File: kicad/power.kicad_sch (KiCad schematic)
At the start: 39 parts, among them Q201 AOD409, U201 TPS54331, U202 AMS1117-3.3

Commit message: Update to v1.1.0
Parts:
- C201: JLCPCB Part # (none) -> C109394
- C202, C203, C210, C211: JLCPCB Part # (none) -> C96446
- C204, C206: JLCPCB Part # (none) -> C57112
- C205: JLCPCB Part # (none) -> C1588
- C207: JLCPCB Part # (none) -> C1679
- C208: JLCPCB Part # (none) -> C107045
- C209, C212: JLCPCB Part # (none) -> C14663
- C213, C214: JLCPCB Part # (none) -> C8020
- D201: JLCPCB Part # (none) -> C110044
- D202: JLCPCB Part # (none) -> C8062
- D203: JLCPCB Part # (none) -> C8678
- D204: JLCPCB Part # (none) -> C142303
- F202: JLCPCB Part # (none) -> C883107
- F501: JLCPCB Part # (none) -> C883133
- L201: JLCPCB Part # (none) -> C68434
- L202: JLCPCB Part # (none) -> C1015
- Q201: JLCPCB Part # (none) -> C36220
- R201, R202, R204, R205, R207: JLCPCB Part # (none) -> C25804
- R203: JLCPCB Part # (none) -> C25803
- R206: JLCPCB Part # (none) -> C23212
- R208: JLCPCB Part # (none) -> C22808
- R209: JLCPCB Part # (none) -> C4177
- R210: JLCPCB Part # (none) -> C23138
- U201: JLCPCB Part # (none) -> C9865
- U202: JLCPCB Part # (none) -> C6186
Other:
- company: BlueDot, Vincenzo Fortunato -> BlueDot Arcade, Vincenzo Fortunato
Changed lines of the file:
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@@
   (title_block
     (title "BD845-PWB SCH")
-    (date "2022-11-27")
-    (rev "1.0.0")
-    (company "BlueDot, Vincenzo Fortunato")
+    (date "2023-06-14")
+    (rev "1.1.0")
+    (company "BlueDot Arcade, Vincenzo Fortunato")
+    (comment 1 "bluedotarcade.com")
   )
   (junction (at 85.09 125.73) (diameter 0) (color 0 0 0 0)
@@
     )
     (property "Datasheet" "~" (at 85.09 121.92 0)
+      (effects (font (size 1.27 1.27)) hide)
+    )
+    (property "JLCPCB Part #" "C25804" (at 85.09 121.92 0)
       (effects (font (size 1.27 1.27)) hide)
     )
@@
     (property "Datasheet" "https://datasheet.lcsc.com/lcsc/1811091710_Alpha---Omega-Semicon-AOD409_C36220.pdf" (at 53.34 55.88 0)
       (effects (font (size 1.27 1.27)) (justify left) hide)
+    )
+    (property "JLCPCB Part #" "C36220" (at 53.34 55.88 0)
+      (effects (font (size 1.27 1.27)) hide)
     )
     (pin "1")
@@
       (effects (font (size 1.27 1.27)) hide)
     )
+    (property "JLCPCB Part #" "C110044" (at 38.1 59.69 0)
+      (effects (font (size 1.27 1.27)) hide)
+    )
     (pin "1")
     (pin "2")
@@
       (effects (font (size 1.27 1.27)))
     )
+    (property "JLCPCB Part #" "C25804" (at 179.07 115.57 0)
+      (effects (font (size 1.27 1.27)) hide)
+    )
     (pin "1")
     (pin "2")
@@
       (effects (font (size 1.27 1.27)) (justify left))
     )
+    (property "JLCPCB Part #" "C8020" (at 118.11 63.5 0)
+      (effects (font (size 1.27 1.27)) hide)
+    )
     (pin "1")
     (pin "2")
@@
       (effects (font (size 1.27 1.27)) hide)
     )
+    (property "JLCPCB Part #" "C96446" (at 189.23 107.95 0)
+      (effects (font (size 1.27 1.27)) hide)
+    )
     (pin "1")
     (pin "2")
@@
     )
     (property "Datasheet" "~" (at 54.61 114.3 0)
+      (effects (font (size 1.27 1.27)) hide)
+    )
+    (property "JLCPCB Part #" "C96446" (at 54.61 114.3 0)
       (effects (font (size 1.27 1.27)) hide)
     )
@@
       (effects (font (size 1.27 1.27)) hide)
     )
+    (property "JLCPCB Part #" "" (at 167.64 58.42 0)
+      (effects (font (size 1.27 1.27)) hide)
+    )
     (pin "1")
     (instances
@@
     )
     (property "Datasheet" "~" (at 166.37 107.95 90)
+      (effects (font (size 1.27 1.27)) hide)
+    )
+    (property "JLCPCB Part #" "C8678" (at 166.37 107.95 0)
       (effects (font (size 1.27 1.27)) hide)
     )
@@
       (effects (font (size 1.27 1.27)) hide)
     )
+    (property "JLCPCB Part #" "C1015" (at 113.03 58.42 0)
+      (effects (font (size 1.27 1.27)) hide)
+    )
     (pin "1")
     (pin "2")
@@
       (effects (font (size 1.27 1.27)) hide)
     )
+    (property "JLCPCB Part #" "C57112" (at 64.77 114.3 0)
+      (effects (font (size 1.27 1.27)) hide)
+    )
     (pin "1")
     (pin "2")
@@
       (effects (font (size 1.27 1.27)) (justify left))
     )
+    (property "JLCPCB Part #" "C23212" (at 115.57 128.27 0)
+      (effects (font (size 1.27 1.27)) hide)
+    )
     (pin "1")
     (pin "2")
@@
     )
     (property "Datasheet" "~" (at 44.45 114.3 0)
+      (effects (font (size 1.27 1.27)) hide)
+    )
+    (property "JLCPCB Part #" "C96446" (at 44.45 114.3 0)
       (effects (font (size 1.27 1.27)) hide)
     )
@@
       (effects (font (size 1.27 1.27)) hide)
     )
+    (property "JLCPCB Part #" "C6186" (at 134.62 58.42 0)
+      (effects (font (size 1.27 1.27)) hide)
+    )
     (pin "1")
     (pin "2")
@@
     )
     (property "Datasheet" "https://www.ti.com/lit/ds/symlink/tps54331.pdf" (at 154.94 127 0)
+      (effects (font (size 1.27 1.27)) hide)
+    )
+    (property "JLCPCB Part #" "C9865" (at 129.54 115.57 0)
       (effects (font (size 1.27 1.27)) hide)
     )
@@
       (effects (font (size 1.27 1.27)) hide)
     )
+    (property "JLCPCB Part #" "C107045" (at 115.57 135.89 0)
+      (effects (font (size 1.27 1.27)) hide)
+    )
     (pin "1")
     (pin "2")
@@
       (effects (font (size 1.27 1.27)) hide)
     )
+    (property "JLCPCB Part #" "C57112" (at 96.52 127 0)
+      (effects (font (size 1.27 1.27)) hide)
+    )
     (pin "1")
     (pin "2")
@@
     (property "Accuracy" "1%" (at 181.61 137.16 0)
       (effects (font (size 1.27 1.27)) (justify left))
+    )
+    (property "JLCPCB Part #" "C4177" (at 179.07 134.62 0)
+      (effects (font (size 1.27 1.27)) hide)
     )
     (pin "1")
@@
       (effects (font (size 1.27 1.27)) hide)
     )
+    (property "JLCPCB Part #" "C25804" (at 53.34 64.77 0)
+      (effects (font (size 1.27 1.27)) hide)
+    )
     (pin "1")
     (pin "2")
@@
     (property "ESR" "10Ω" (at 153.67 66.04 0)
       (effects (font (size 1.27 1.27)) (justify left))
+    )
+    (property "JLCPCB Part #" "C8020" (at 151.13 63.5 0)
+      (effects (font (size 1.27 1.27)) hide)
     )
     (pin "1")
@@
       (effects (font (size 1.27 1.27)) hide)
     )
+    (property "JLCPCB Part #" "C883107" (at 160.02 58.42 0)
+      (effects (font (size 1.27 1.27)) hide)
+    )
     (pin "1")
     (pin "2")
@@
       (effects (font (size 1.27 1.27)) hide)
     )
+    (property "JLCPCB Part #" "C8062" (at 60.96 57.15 0)
+      (effects (font (size 1.27 1.27)) hide)
+    )
     (pin "1")
     (pin "2")
@@
     (property "Accuracy" "1%" (at 182.88 128.27 0)
       (effects (font (size 1.27 1.27)))
+    )
+    (property "JLCPCB Part #" "C22808" (at 179.07 125.73 0)
+      (effects (font (size 1.27 1.27)) hide)
     )
     (pin "1")
@@
       (effects (font (size 1.27 1.27)) hide)
     )
+    (property "JLCPCB Part #" "C25803" (at 85.09 114.3 0)
+      (effects (font (size 1.27 1.27)) hide)
+    )
     (pin "1")
     (pin "2")
@@
       (effects (font (size 1.27 1.27)) hide)
     )
+    (property "JLCPCB Part #" "C23138" (at 204.47 69.85 0)
+      (effects (font (size 1.27 1.27)) hide)
+    )
     (pin "1")
     (pin "2")
@@
       (effects (font (size 1.27 1.27)))
     )
+    (property "JLCPCB Part #" "C68434" (at 172.72 102.87 0)
+      (effects (font (size 1.27 1.27)) hide)
+    )
     (pin "1")
     (pin "2")
@@
     )
     (property "Datasheet" "~" (at 107.95 63.5 0)
+      (effects (font (size 1.27 1.27)) hide)
+    )
+    (property "JLCPCB Part #" "C14663" (at 107.95 63.5 0)
       (effects (font (size 1.27 1.27)) hide)
     )
@@
       (effects (font (size 1.27 1.27)) hide)
     )
+    (property "JLCPCB Part #" "C142303" (at 204.47 49.53 0)
+      (effects (font (size 1.27 1.27)) hide)
+    )
     (pin "1")
     (pin "2")
@@
       (effects (font (size 1.27 1.27)) hide)
     )
+    (property "JLCPCB Part #" "C25804" (at 74.93 129.54 0)
+      (effects (font (size 1.27 1.27)) hide)
+    )
     (pin "1")
     (pin "2")
@@
     )
     (property "Datasheet" "~" (at 74.93 114.3 0)
+      (effects (font (size 1.27 1.27)) hide)
+    )
+    (property "JLCPCB Part #" "C1588" (at 74.93 114.3 0)
       (effects (font (size 1.27 1.27)) hide)
     )
@@
       (effects (font (size 1.27 1.27)) hide)
     )
+    (property "JLCPCB Part #" "C883133" (at 38.1 110.49 0)
+      (effects (font (size 1.27 1.27)) hide)
+    )
     (pin "1")
     (pin "2")
@@
       (effects (font (size 1.27 1.27)) hide)
     )
+    (property "JLCPCB Part #" "C96446" (at 199.39 107.95 0)
+      (effects (font (size 1.27 1.27)) hide)
+    )
     (pin "1")
     (pin "2")
@@
     (property "ESR" "1mΩ" (at 156.21 106.68 90)
       (effects (font (size 1.27 1.27)))
+    )
+    (property "JLCPCB Part #" "C14663" (at 156.21 110.49 0)
+      (effects (font (size 1.27 1.27)) hide)
     )
     (pin "1")
@@
       (effects (font (size 1.27 1.27)) hide)
     )
+    (property "JLCPCB Part #" "" (at 72.39 53.34 0)
+      (effects (font (size 1.27 1.27)) hide)
+    )
     (pin "1")
     (instances
@@
     )
     (property "Datasheet" "~" (at 85.09 129.54 0)
+      (effects (font (size 1.27 1.27)) hide)
+    )
+    (property "JLCPCB Part #" "C25804" (at 85.09 129.54 0)
       (effects (font (size 1.27 1.27)) hide)
     )
@@
       (effects (font (size 1.27 1.27)) hide)
     )
+    (property "JLCPCB Part #" "" (at 199.39 102.87 0)
+      (effects (font (size 1.27 1.27)) hide)
+    )
     (pin "1")
     (instances
@@
     )
     (property "Datasheet" "~" (at 106.68 135.89 0)
+      (effects (font (size 1.27 1.27)) hide)
+    )
+    (property "JLCPCB Part #" "C1679" (at 106.68 135.89 0)
       (effects (font (size 1.27 1.27)) hide)
     )
@@
     )
     (property "Datasheet" "~" (at 77.47 68.58 0)
+      (effects (font (size 1.27 1.27)) hide)
+    )
+    (property "JLCPCB Part #" "" (at 72.39 68.58 0)
       (effects (font (size 1.27 1.27)) hide)
     )
@@
       (effects (font (size 1.27 1.27)) hide)
     )
+    (property "JLCPCB Part #" "C109394" (at 72.39 60.96 0)
+      (effects (font (size 1.27 1.27)) hide)
+    )

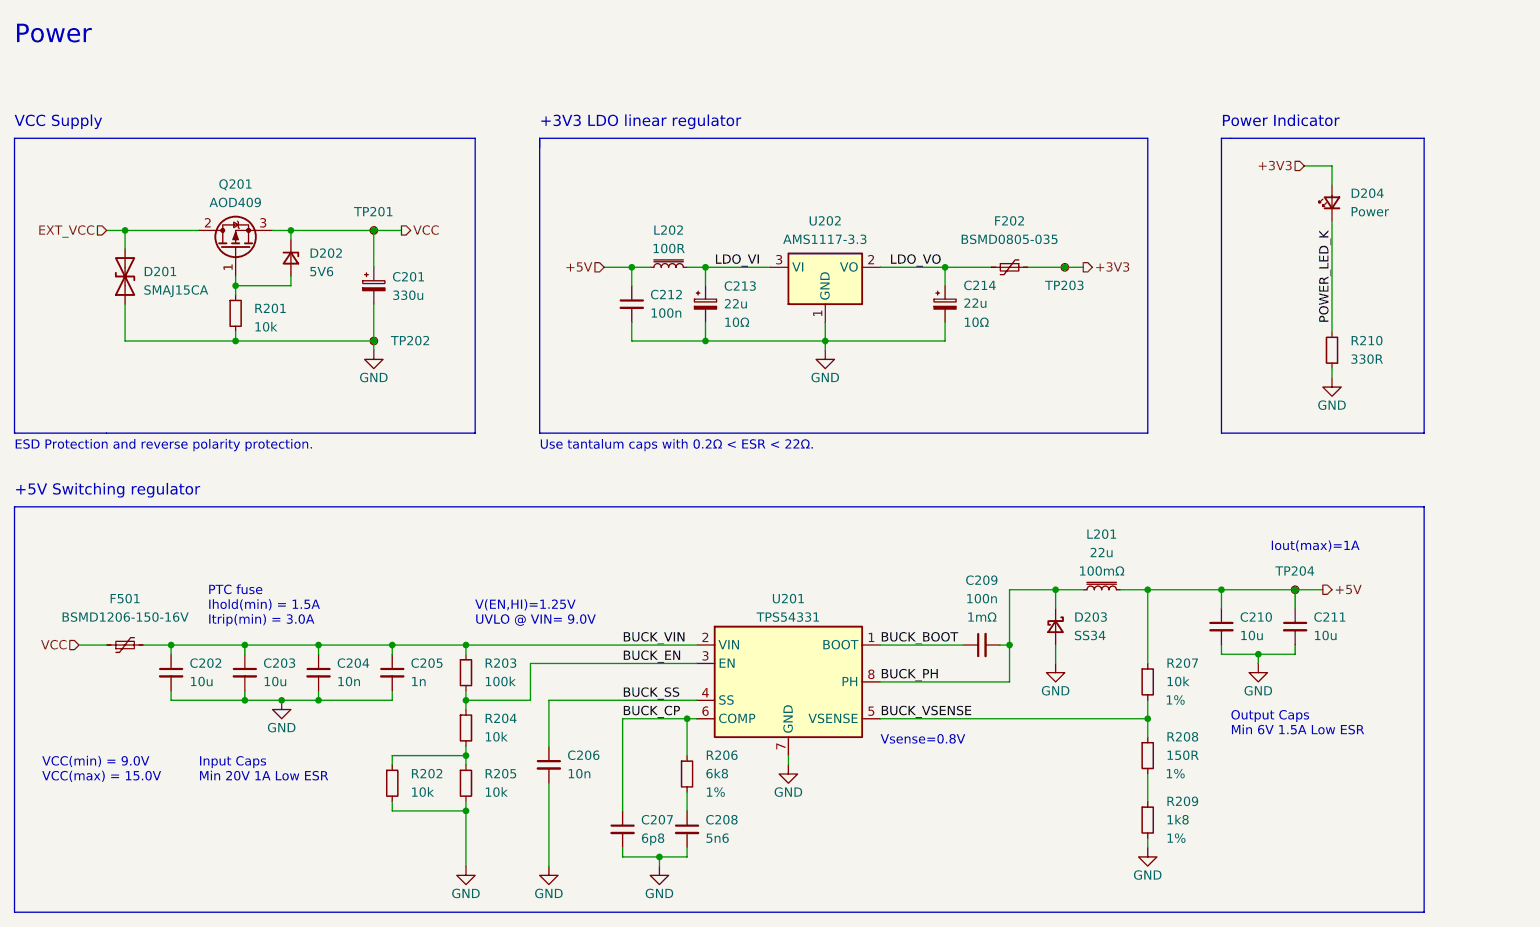
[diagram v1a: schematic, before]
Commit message: Split 5n6 capacitor into two separate caps
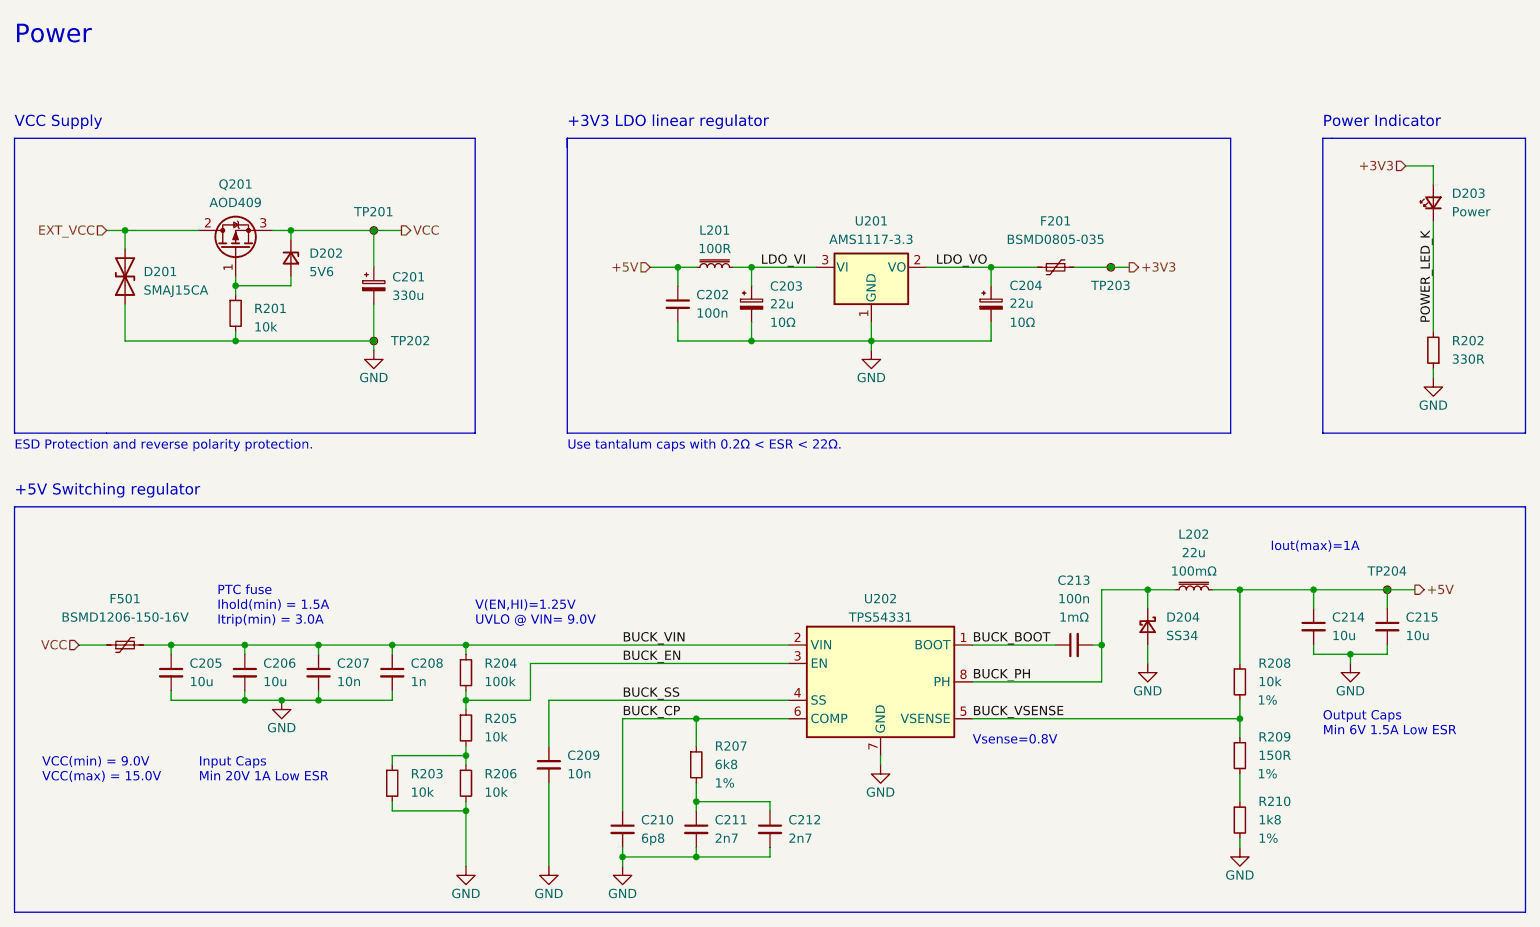
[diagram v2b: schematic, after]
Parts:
- added C212: 2n7, Capacitor_SMD:C_0603_1608Metric, symbol Device:C_Small
- C211: renamed from C208; value 5n6 -> 2n7; JLCPCB Part # C107045 -> C1609
- renumbered C212 to C202, C213 to C203, C214 to C204, C202 to C205, C203 to C206, C204 to C207, C205 to C208, C206 to C209, C207 to C210, C209 to C213, C210 to C214, C211 to C215, D204 to D203, D203 to D204, F202 to F201, L202 to L201, L201 to L202, R210 to R202, R202 to R203, R203 to R204, R204 to R205, R205 to R206, R206 to R207, R207 to R208, R208 to R209, R209 to R210, U202 to U201, U201 to U202
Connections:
- net GND: now also C212.2
- net at C211.1, R207.2: now also C212.1
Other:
- moved on the sheet: C202, C203, C204, C211, C213, C214, C215, D203, D204, F201, L201, L202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

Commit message: Change light driver to a self-protected mosfet. Remove unnecessary fuses. Change 74HC595 to low input voltage equivalent. Change LED resistors to 1k. Power lights shift register with +5V.
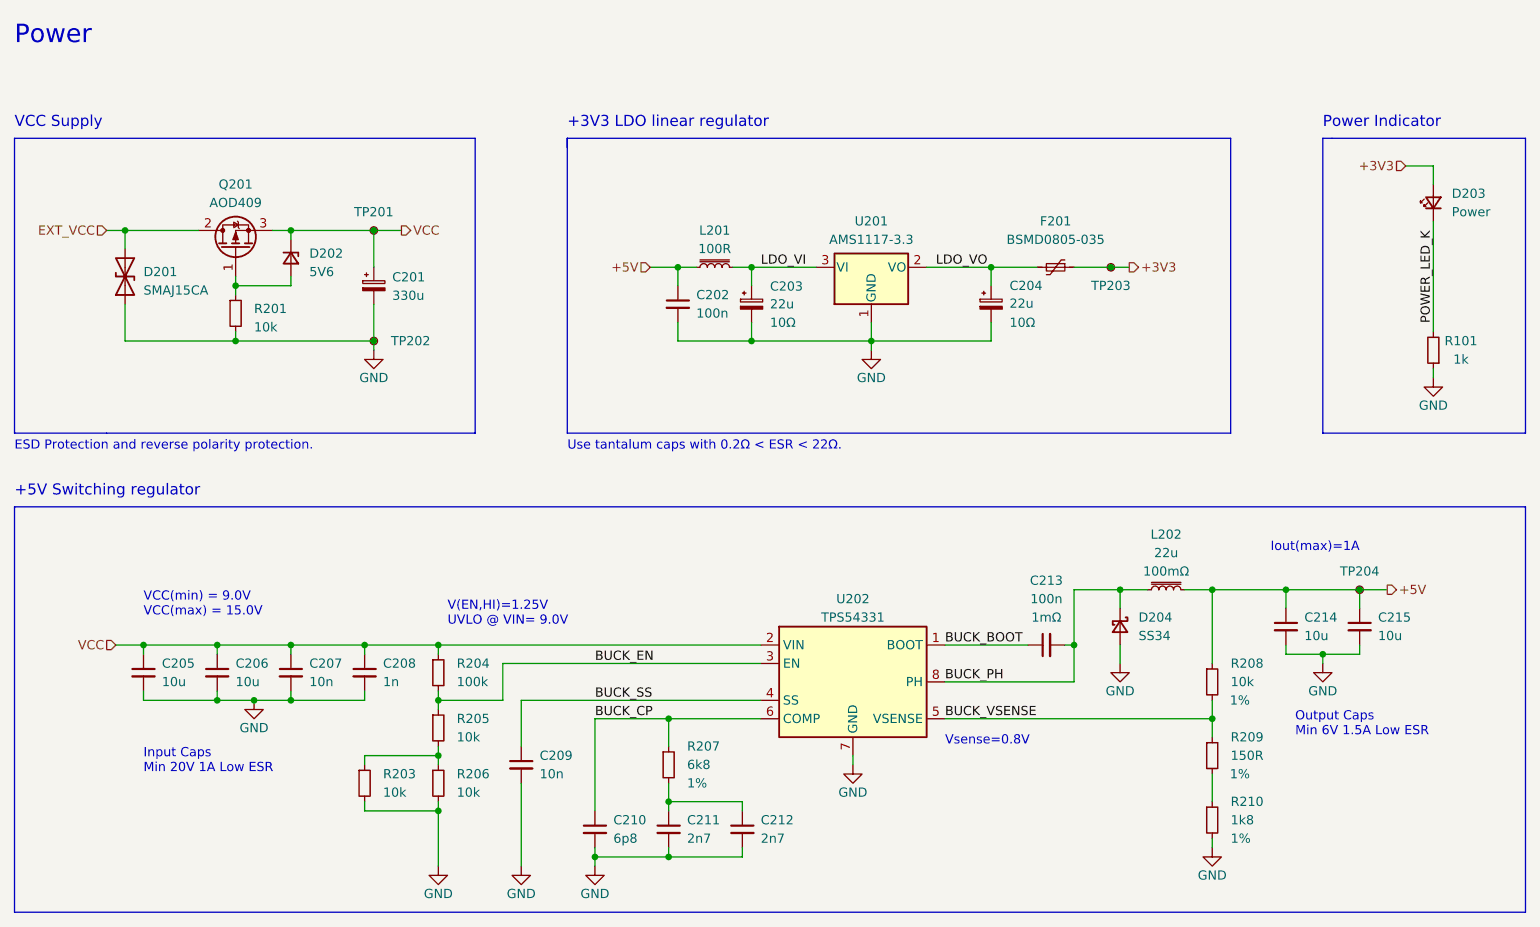
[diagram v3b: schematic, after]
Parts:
- removed F501: BSMD1206-150-16V, Fuse:Fuse_1206_3216Metric_Pad1.42x1.75mm_HandSolder, symbol Device:Polyfuse_Small
- removed R202: 330R, Resistor_SMD:R_0603_1608Metric, symbol Device:R_Small
- added R101: 1k, Resistor_SMD:R_0603_1608Metric, symbol Device:R_Small
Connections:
- net BUCK_VIN is gone; now on net VCC: C205.1, C206.1, C207.1, C208.1, R204.1, U202.2 (VIN)
- net GND: now also R101.1
- net POWER_LED_K: now also R101.2
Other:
- note removed: "PTC fuse Ihold(min) = 1.5A Itrip(min) = 3.0A"
- moved on the sheet: C205, C206, C207, C208, C209, C210, C211, C212, C213, C214, C215, D204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
